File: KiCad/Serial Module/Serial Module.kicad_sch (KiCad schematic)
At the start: 0 parts

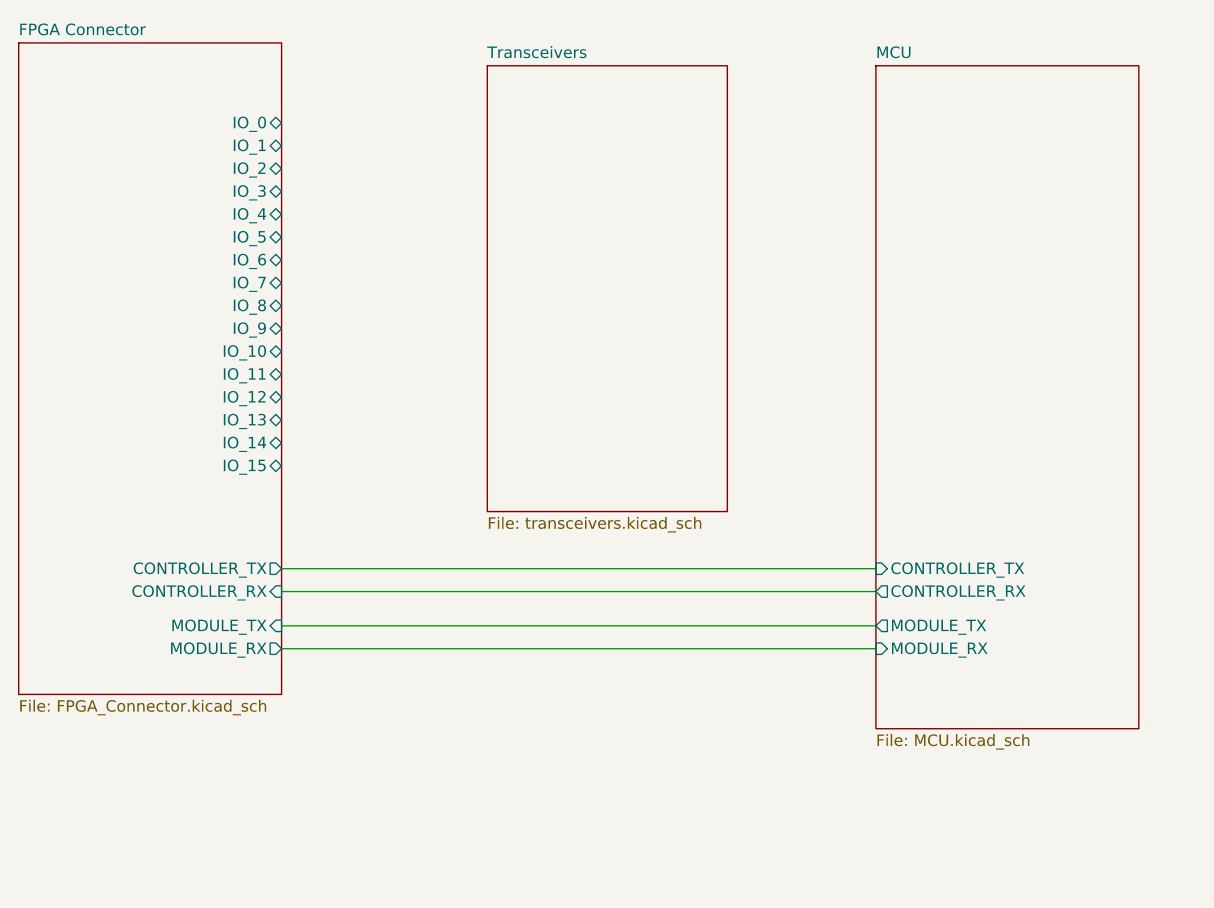
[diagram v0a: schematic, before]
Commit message: update serial module and backplane hw
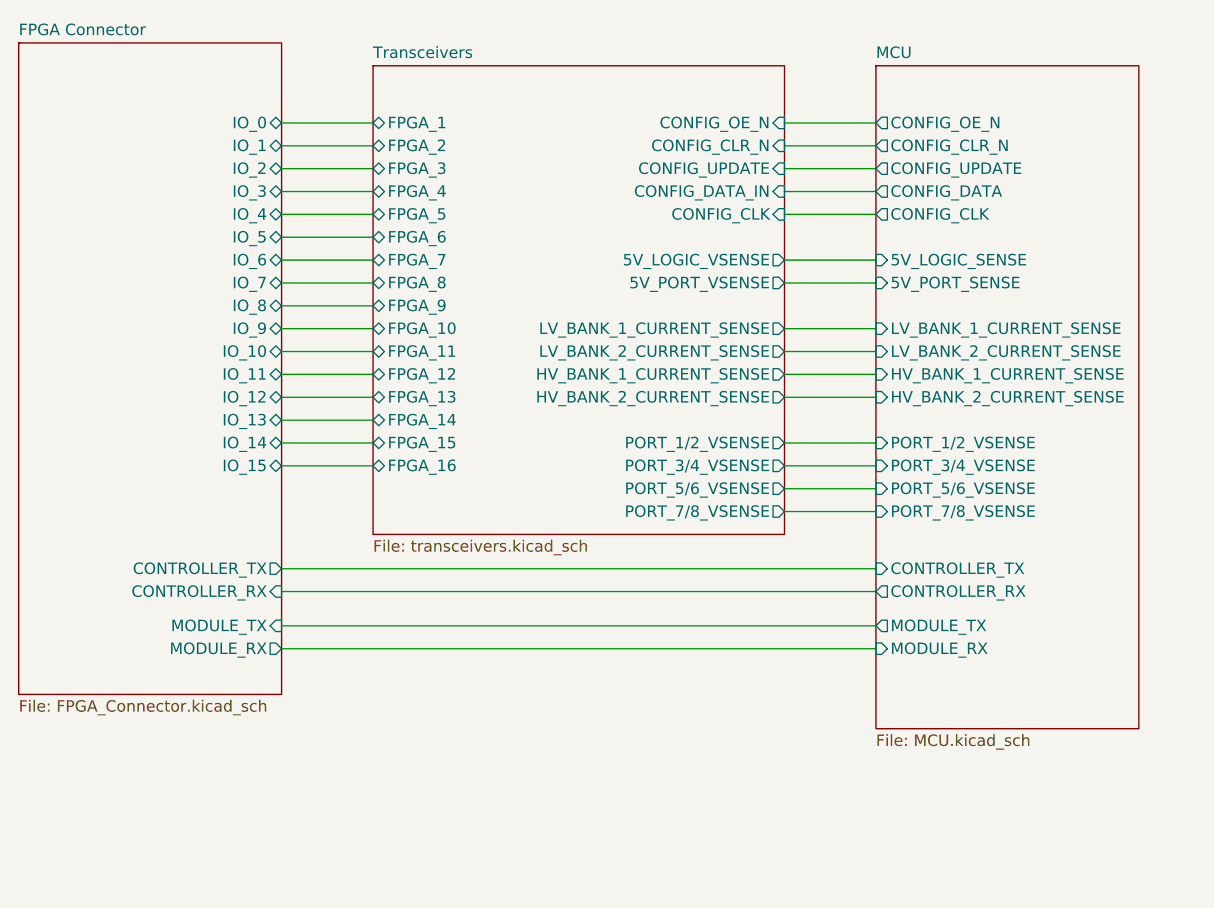
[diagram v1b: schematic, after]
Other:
- sheet MCU ports: added 5V_LOGIC_SENSE, 5V_PORT_SENSE, CONFIG_CLK, CONFIG_CLR_N, CONFIG_DATA, CONFIG_OE_N, CONFIG_UPDATE, HV_BANK_1_CURRENT_SENSE, HV_BANK_2_CURRENT_SENSE, LV_BANK_1_CURRENT_SENSE, LV_BANK_2_CURRENT_SENSE, PORT_1/2_VSENSE, PORT_3/4_VSENSE, PORT_5/6_VSENSE, PORT_7/8_VSENSE; removed none
- sheet Transceivers ports: added 5V_LOGIC_VSENSE, 5V_PORT_VSENSE, CONFIG_CLK, CONFIG_CLR_N, CONFIG_DATA_IN, CONFIG_OE_N, CONFIG_UPDATE, FPGA_1, FPGA_10, FPGA_11, FPGA_12, FPGA_13, FPGA_14, FPGA_15, FPGA_16, FPGA_2, FPGA_3, FPGA_4, FPGA_5, FPGA_6, FPGA_7, FPGA_8, FPGA_9, HV_BANK_1_CURRENT_SENSE, HV_BANK_2_CURRENT_SENSE, LV_BANK_1_CURRENT_SENSE, LV_BANK_2_CURRENT_SENSE, PORT_1/2_VSENSE, PORT_3/4_VSENSE, PORT_5/6_VSENSE, PORT_7/8_VSENSE; removed none

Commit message: add current limit and sense parts, add possible endat solution
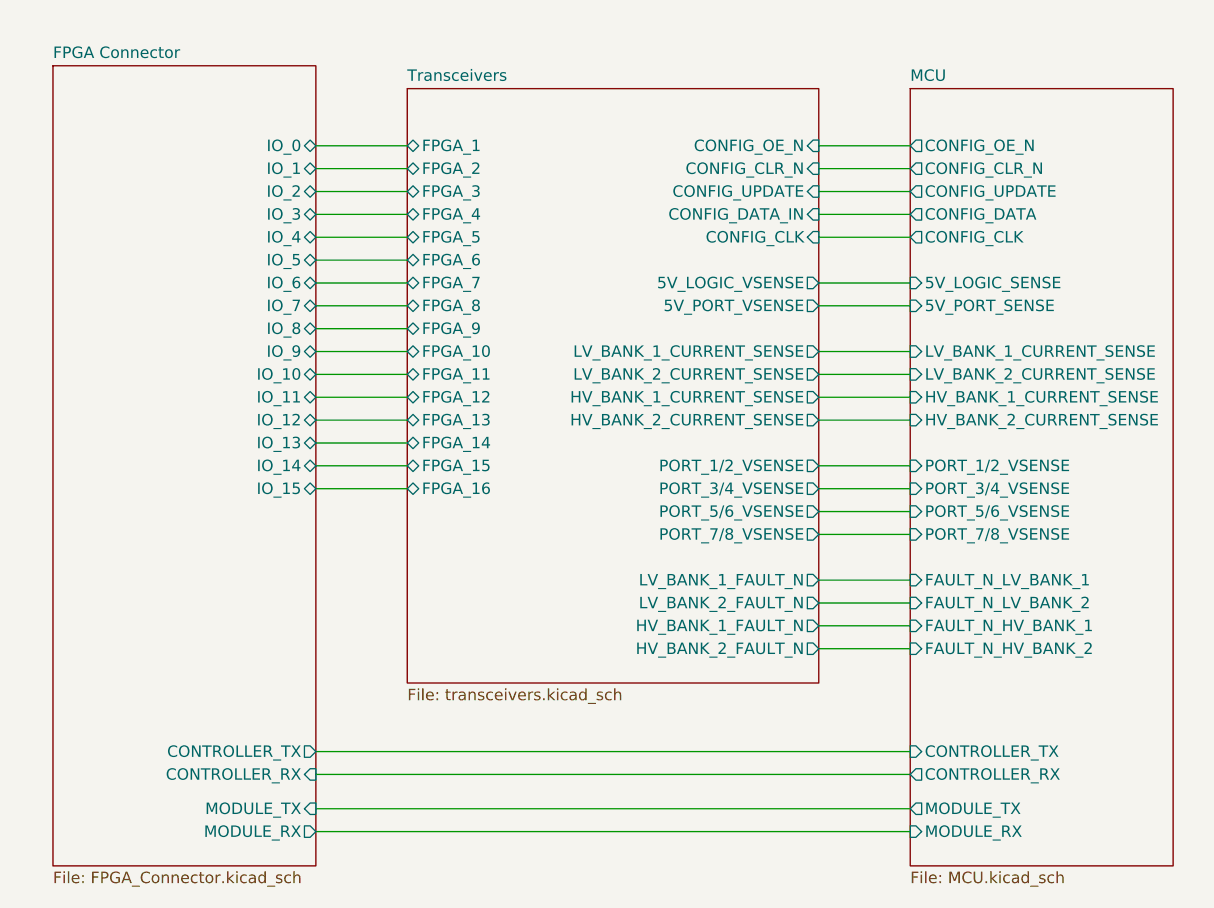
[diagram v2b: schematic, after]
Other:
- sheet MCU ports: added FAULT_N_HV_BANK_1, FAULT_N_HV_BANK_2, FAULT_N_LV_BANK_1, FAULT_N_LV_BANK_2; removed none
- sheet Transceivers ports: added HV_BANK_1_FAULT_N, HV_BANK_2_FAULT_N, LV_BANK_1_FAULT_N, LV_BANK_2_FAULT_N; removed none
